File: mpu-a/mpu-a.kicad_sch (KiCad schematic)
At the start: 29 parts, among them J1 Conn_01x08, U1 W65C02SxP, U2 74HC245, U3 74HC00, U4 74HC245, U5 74HC245, U6 74HC245, U7 74HC138, X1 1MHz

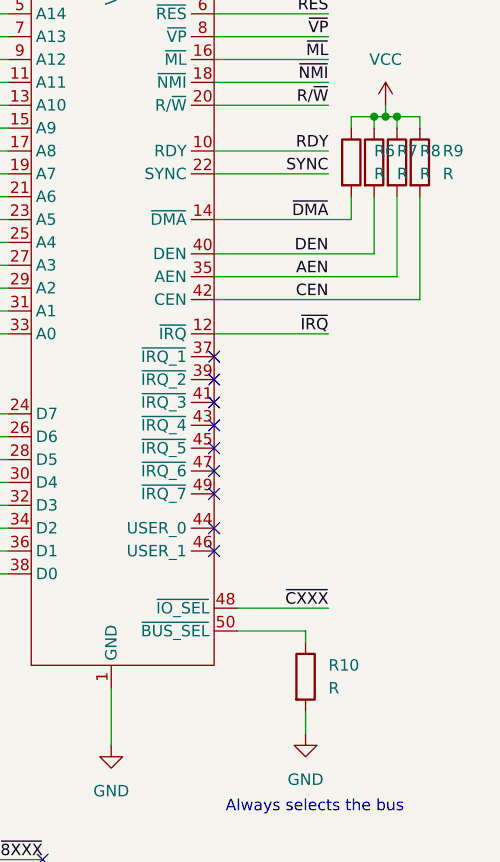
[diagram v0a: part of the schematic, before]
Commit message: Specify resistors values to MPU-A
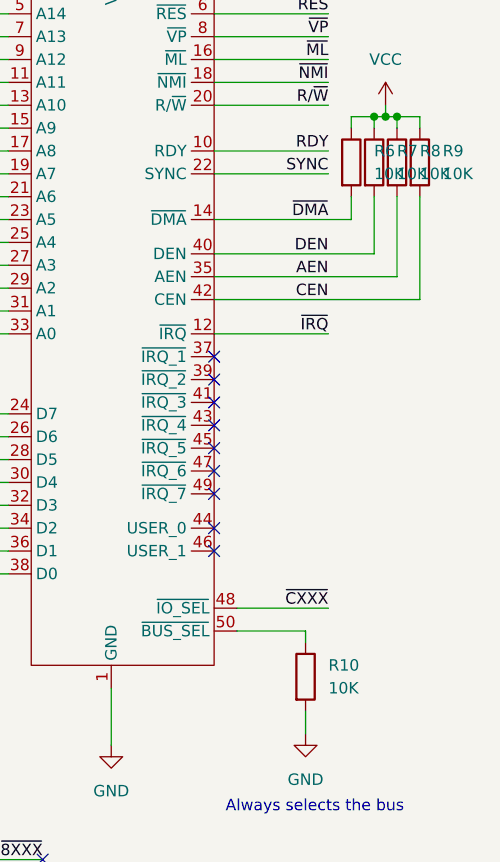
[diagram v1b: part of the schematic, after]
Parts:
- R10, R6, R7, R8, R9: value R -> 10K
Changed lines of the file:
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@@
       (effects (font (size 1.27 1.27)) (justify left))
     )
-    (property "Value" "R" (at 280.67 59.69 0)
+    (property "Value" "10K" (at 280.67 59.69 0)
       (effects (font (size 1.27 1.27)) (justify left))
     )
@@
       (effects (font (size 1.27 1.27)) (justify left))
     )
-    (property "Value" "R" (at 273.05 59.69 0)
+    (property "Value" "10K" (at 273.05 59.69 0)
       (effects (font (size 1.27 1.27)) (justify left))
     )
@@
       (effects (font (size 1.27 1.27)) (justify left))
     )
-    (property "Value" "R" (at 275.59 59.69 0)
+    (property "Value" "10K" (at 275.59 59.69 0)
       (effects (font (size 1.27 1.27)) (justify left))
     )
@@
       (effects (font (size 1.27 1.27)) (justify left))
     )
-    (property "Value" "R" (at 278.13 59.69 0)
+    (property "Value" "10K" (at 278.13 59.69 0)
       (effects (font (size 1.27 1.27)) (justify left))
     )
@@
       (effects (font (size 1.27 1.27)) (justify left))
     )
-    (property "Value" "R" (at 267.97 116.84 0)
-      (effects (font (size 1.27 1.27)) (justify left))
-    )
+    (property "Value" "10K" (at 267.97 116.84 0)
+      (effects (font (size 1.27 1.27)) (justify left))
+    )
